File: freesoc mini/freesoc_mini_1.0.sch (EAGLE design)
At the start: 50 parts, among them IC1 CY7C68013A-56QFNLFXC, IC2 24LC00OT, Y1 XRCGB24M000F0L00R0

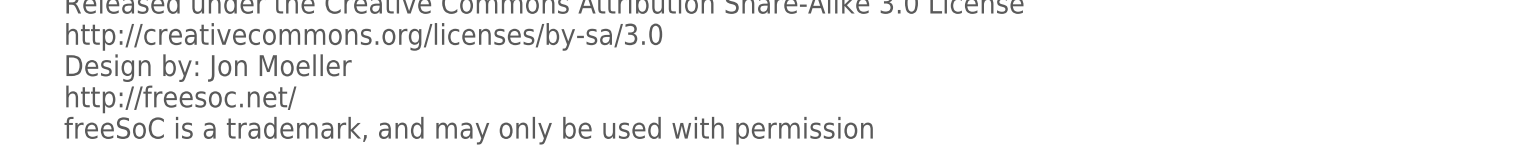
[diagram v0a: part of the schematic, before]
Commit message: DFM changes to freesoc mini board
All vias tented.

Updated land pattern for FX2 and PSoC for improved reliability and
smaller defect rate.
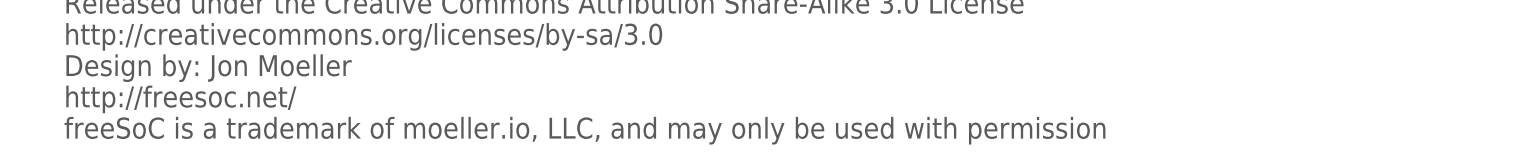
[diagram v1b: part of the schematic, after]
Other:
- note added: "freeSoC is a trademark of moeller.io, LLC, and may only be used with permission"
- note removed: "freeSoC is a trademark, and may only be used with permission"
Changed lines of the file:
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@@
 <?xml version="1.0" encoding="utf-8"?>
 <!DOCTYPE eagle SYSTEM "eagle.dtd">
-<eagle version="6.1">
+<eagle version="6.2">
 <drawing>
 <settings>
@@
 <text x="2.54" y="-119.38" size="5.08" layer="97" font="vector">Design by: Jon Moeller</text>
 <text x="2.54" y="-127" size="5.08" layer="97" font="vector">http://freesoc.net/</text>
-<text x="2.54" y="-134.62" size="5.08" layer="97" font="vector">freeSoC is a trademark, and may only be used with permission</text>
+<text x="2.54" y="-134.62" size="5.08" layer="97" font="vector">freeSoC is a trademark of moeller.io, LLC, and may only be used with permission</text>
 <text x="2.54" y="-93.98" size="6.4516" layer="97" font="vector">freeSoC Mini Development Kit v1.0</text>
 <text x="40.64" y="-87.122" size="1.778" layer="97">TM</text>

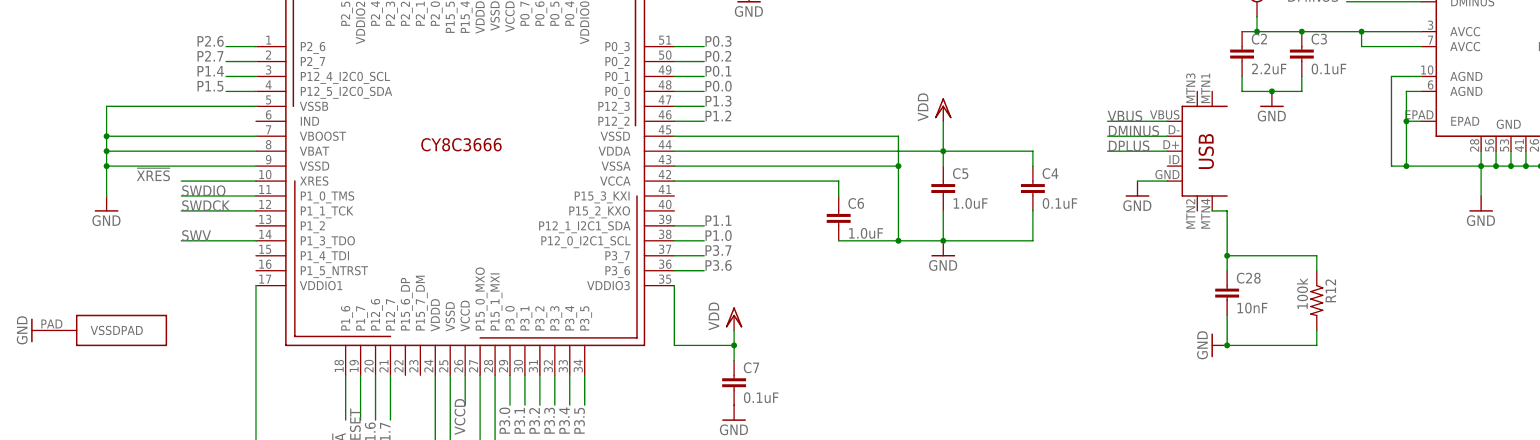
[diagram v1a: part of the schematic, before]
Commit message: More DFM changes for freesoc mini
Updated FX2 QFN thermal pad to meet cypress spec.

Updated PSoC QFN thermal pad to meet cypress spec.

Added tented vias on thermal pad for both chips, proper solder paste
stencil, and removed solder mask from bottom of vias to prevent
outgassing.
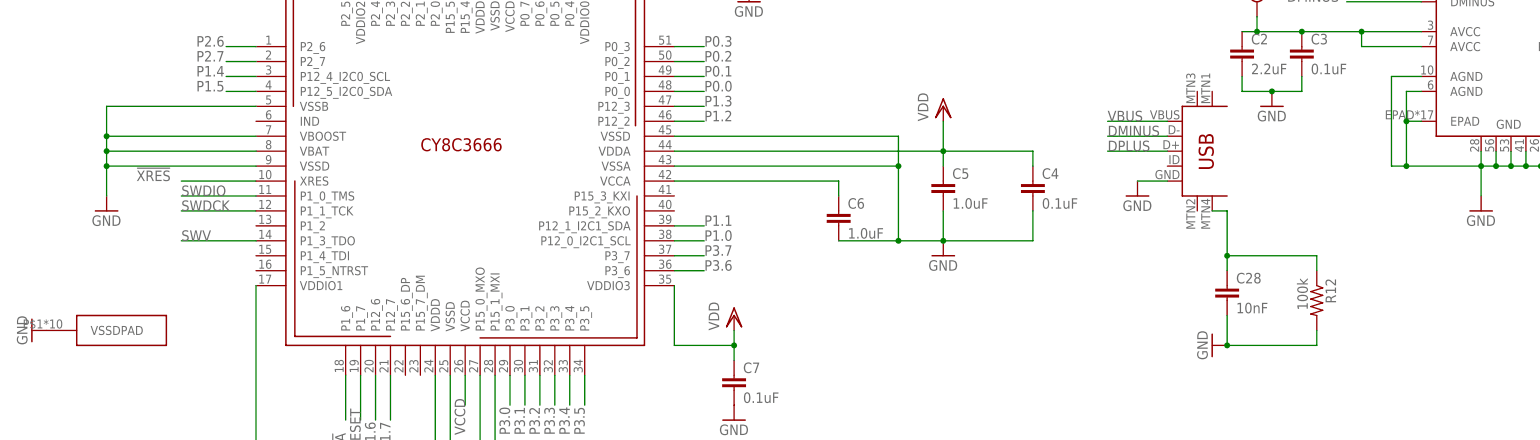
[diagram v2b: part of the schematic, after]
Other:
- moved on the sheet: IC1
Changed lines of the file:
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@@
 <grid distance="0.1" unitdist="inch" unit="inch" style="lines" multiple="1" display="no" altdistance="0.01" altunitdist="inch" altunit="inch"/>
 <layers>
-<layer number="1" name="Top" color="4" fill="1" visible="no" active="no"/>
-<layer number="2" name="Route2" color="11" fill="1" visible="no" active="no"/>
-<layer number="3" name="Route3" color="4" fill="3" visible="no" active="no"/>
-<layer number="14" name="Route14" color="1" fill="6" visible="no" active="no"/>
-<layer number="15" name="Route15" color="13" fill="1" visible="no" active="no"/>
-<layer number="16" name="Bottom" color="1" fill="1" visible="no" active="no"/>
-<layer number="17" name="Pads" color="2" fill="1" visible="no" active="no"/>
-<layer number="18" name="Vias" color="2" fill="1" visible="no" active="no"/>
-<layer number="19" name="Unrouted" color="14" fill="1" visible="no" active="no"/>
-<layer number="20" name="Dimension" color="15" fill="1" visible="no" active="no"/>
-<layer number="21" name="tPlace" color="7" fill="1" visible="no" active="no"/>
-<layer number="22" name="bPlace" color="7" fill="1" visible="no" active="no"/>
-<layer number="23" name="tOrigins" color="15" fill="1" visible="no" active="no"/>
-<layer number="24" name="bOrigins" color="15" fill="1" visible="no" active="no"/>
-<layer number="25" name="tNames" color="15" fill="1" visible="no" active="no"/>
-<layer number="26" name="bNames" color="7" fill="1" visible="no" active="no"/>
-<layer number="27" name="tValues" color="7" fill="1" visible="no" active="no"/>
-<layer number="28" name="bValues" color="7" fill="1" visible="no" active="no"/>
+<layer number="1" name="Top" color="4" fill="1" visible="yes" active="no"/>
+<layer number="2" name="Route2" color="11" fill="1" visible="yes" active="no"/>
+<layer number="3" name="Route3" color="4" fill="3" visible="yes" active="no"/>
+<layer number="14" name="Route14" color="1" fill="6" visible="yes" active="no"/>
+<layer number="15" name="Route15" color="13" fill="1" visible="yes" active="no"/>
+<layer number="16" name="Bottom" color="1" fill="1" visible="yes" active="no"/>
+<layer number="17" name="Pads" color="2" fill="1" visible="yes" active="no"/>
+<layer number="18" name="Vias" color="2" fill="1" visible="yes" active="no"/>
+<layer number="19" name="Unrouted" color="14" fill="1" visible="yes" active="no"/>
+<layer number="20" name="Dimension" color="15" fill="1" visible="yes" active="no"/>
+<layer number="21" name="tPlace" color="7" fill="1" visible="yes" active="no"/>
+<layer number="22" name="bPlace" color="7" fill="1" visible="yes" active="no"/>
+<layer number="23" name="tOrigins" color="15" fill="1" visible="yes" active="no"/>
+<layer number="24" name="bOrigins" color="15" fill="1" visible="yes" active="no"/>
+<layer number="25" name="tNames" color="15" fill="1" visible="yes" active="no"/>
+<layer number="26" name="bNames" color="7" fill="1" visible="yes" active="no"/>
+<layer number="27" name="tValues" color="7" fill="1" visible="yes" active="no"/>
+<layer number="28" name="bValues" color="7" fill="1" visible="yes" active="no"/>
 <layer number="29" name="tStop" color="10" fill="9" visible="no" active="no"/>
 <layer number="30" name="bStop" color="10" fill="9" visible="no" active="no"/>
@@
 <layer number="35" name="tGlue" color="7" fill="4" visible="no" active="no"/>
 <layer number="36" name="bGlue" color="7" fill="5" visible="no" active="no"/>
-<layer number="37" name="tTest" color="7" fill="1" visible="no" active="no"/>
-<layer number="38" name="bTest" color="7" fill="1" visible="no" active="no"/>
+<layer number="37" name="tTest" color="7" fill="1" visible="yes" active="no"/>
+<layer number="38" name="bTest" color="7" fill="1" visible="yes" active="no"/>
 <layer number="39" name="tKeepout" color="4" fill="11" visible="no" active="no"/>
 <layer number="40" name="bKeepout" color="1" fill="11" visible="no" active="no"/>
@@
 <layer number="44" name="Drills" color="7" fill="1" visible="no" active="no"/>
 <layer number="45" name="Holes" color="7" fill="1" visible="no" active="no"/>
-<layer number="46" name="Milling" color="3" fill="1" visible="no" active="no"/>
-<layer number="47" name="Measures" color="7" fill="1" visible="no" active="no"/>
-<layer number="48" name="Document" color="7" fill="1" visible="no" active="no"/>
-<layer number="49" name="Reference" color="7" fill="1" visible="no" active="no"/>
-<layer number="50" name="dxf" color="7" fill="1" visible="no" active="no"/>
-<layer number="51" name="tDocu" color="7" fill="1" visible="no" active="no"/>
-<layer number="52" name="bDocu" color="7" fill="1" visible="no" active="no"/>
-<layer number="53" name="tGND_GNDA" color="7" fill="9" visible="no" active="no"/>
-<layer number="54" name="bGND_GNDA" color="1" fill="9" visible="no" active="no"/>
-<layer number="56" name="wert" color="7" fill="1" visible="no" active="no"/>
+<layer number="46" name="Milling" color="3" fill="1" visible="yes" active="no"/>
+<layer number="47" name="Measures" color="7" fill="1" visible="yes" active="no"/>
+<layer number="48" name="Document" color="7" fill="1" visible="yes" active="no"/>
+<layer number="49" name="Reference" color="7" fill="1" visible="yes" active="no"/>
+<layer number="50" name="dxf" color="7" fill="1" visible="yes" active="no"/>
+<layer number="51" name="tDocu" color="7" fill="1" visible="yes" active="no"/>
+<layer number="52" name="bDocu" color="7" fill="1" visible="yes" active="no"/>
+<layer number="53" name="tGND_GNDA" color="7" fill="9" visible="yes" active="no"/>
+<layer number="54" name="bGND_GNDA" color="1" fill="9" visible="yes" active="no"/>
+<layer number="56" name="wert" color="7" fill="1" visible="yes" active="no"/>
 <layer number="91" name="Nets" color="2" fill="1" visible="yes" active="yes"/>
 <layer number="92" name="Busses" color="1" fill="1" visible="yes" active="yes"/>
